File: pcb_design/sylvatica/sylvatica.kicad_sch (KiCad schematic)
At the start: 120 parts, among them J1 USB_C_Receptacle, J2 USB_C_Receptacle, J3 USB_C_Receptacle, J4 USB_C_Receptacle, J5 Conn_02x13_Odd_Even, J6 Conn_01x04_Female, J7 Conn_01x06_Female, J9 Conn_01x06_Female, Q1 Q_NMOS_GSD, Q2 Q_NMOS_GSD, SW1 SW_Push, U1 PGA113, U10 dsPIC33EP512MC806, U11 SiP32431, U12 LP2985-5.0, U13 REF2033, U14 OPA320, U15 SiP32431, U16 SiP32431, U17 SiP32431, U18 SiP32431, U19 ADM7170, U2 PGA113, U20 MCP2542FD, U21 TPS737, U22 SiP32431, U3 PGA113, U4 PGA113, U5 PGA113, U6 PGA113, U7 PGA113, U8 PGA113, U9 ADS8332, Y1 Crystal_GND24

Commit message: Update.
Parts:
- added J8: Conn_01x04_Female, Connector_PinSocket_2.54mm:PinSocket_1x04_P2.54mm_Vertical, symbol Connector:Conn_01x04_Female
- C20: symbol Device:CP -> Device:C
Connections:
- net BLINK: now also U10.63 (AN27PWM2H/PMD3/RPI83/RE3); no longer U10.64 (AN28/PWM3L/PMD4/RP84/RE4)
- net EV1: now also J1.A7 (D-), J1.B7 (D-); no longer J1.A10 (RX2-), J1.B10 (RX1-)
- net EV2: now also J2.A7 (D-), J2.B7 (D-); no longer J2.A10 (RX2-), J2.B10 (RX1-)
- net EV3: now also J3.A7 (D-), J3.B7 (D-); no longer J3.A10 (RX2-), J3.B10 (RX1-)
- net EV4: now also J4.A7 (D-), J4.B7 (D-); no longer J4.A10 (RX2-), J4.B10 (RX1-)
- net OW1: now also J1.A6 (D+), J1.B6 (D+), U10.22 (AN9/PMA7/RPI41/RB9); no longer J1.A3 (TX1-), J1.B3 (TX2-)
- net OW2: now also J2.A6 (D+), J2.B6 (D+), U10.21 (AN8/PMA6/RPI40/RB8); no longer J2.A3 (TX1-), J2.B3 (TX2-)
- net OW3: now also J3.A6 (D+), J3.B6 (D+), U10.11 (AN5/C1IN1+/RPI37/RB5); no longer J3.A3 (TX1-), J3.B3 (TX2-)
- net OW4: now also J4.A6 (D+), J4.B6 (D+), U10.64 (AN28/PWM3L/PMD4/RP84/RE4); no longer J4.A3 (TX1-), J4.B3 (TX2-)
- net REF_C2: now also U10.27 (TCK/AN12/PMA11/RPI44/RB12); no longer U10.29 (AN14/PMA1/RPI46/RB14)
- net SCL1: now also J1.A10 (RX2-), J1.B10 (RX1-), J2.A10 (RX2-), J2.B10 (RX1-), J3.A10 (RX2-), J3.B10 (RX1-), J4.A10 (RX2-), J4.B10 (RX1-); no longer J1.A7 (D-), J1.B7 (D-), J2.A7 (D-), J2.B7 (D-), J3.A7 (D-), J3.B7 (D-), J4.A7 (D-), J4.B7 (D-)
- net SDA1: now also J1.A3 (TX1-), J1.B3 (TX2-), J2.A3 (TX1-), J2.B3 (TX2-), J3.A3 (TX1-), J3.B3 (TX2-), J4.A3 (TX1-), J4.B3 (TX2-); no longer J1.A6 (D+), J1.B6 (D+), J2.A6 (D+), J2.B6 (D+), J3.A6 (D+), J3.B6 (D+), J4.A6 (D+), J4.B6 (D+)
- net S_PS_SW2: now also U10.15 (PGEC3/AN1/VREF-/RPI33/RB1); no longer U10.12 (AN4/C1IN2-/RPI36/RB4)
- net ~{INT2}: now also U10.16 (PGED3/AN0/VREF+/RPI32/RB0); no longer U10.13 (AN3/C2IN1+/VPIO/RPI35/RB3)
- net OW5: now reaches U10.23 (TMS/AN10/PMA13/RPI42/RB10)
- net OW5: now also J8.1 (Pin_1)
- net OW6: now reaches U10.28 (TDI/AN13/PMA10/RPI45/RB13)
- net OW6: now also J8.2 (Pin_2)
- net +3V3 renamed +3.3V
- net AS_PS renamed S_PS
- net AS_PS2 renamed S_PS2
- net CAN_C1: no longer names the net of J5.23 (Pin_23)
- net PGM: no longer names the net of J9.6 (Pin_6)
- new net OW7: J8.3 (Pin_3), U10.12 (AN4/C1IN2-/RPI36/RB4)
- new net OW8: J8.4 (Pin_4), U10.13 (AN3/C2IN1+/VPIO/RPI35/RB3)
- no-connect marks 4 -> 39
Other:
- moved on the sheet: C45

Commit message: New and updated board designs.
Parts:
- removed J5: Conn_02x13_Odd_Even, Connector_PinHeader_2.54mm:PinHeader_2x13_P2.54mm_Vertical, symbol Connector_Generic:Conn_02x13_Odd_Even
- removed J6, J8: Conn_01x04_Female, Connector_PinSocket_2.54mm:PinSocket_1x04_P2.54mm_Vertical, symbol Connector:Conn_01x04_Female
- removed J7: Conn_01x06_Female, Connector_PinSocket_2.54mm:PinSocket_1x06_P2.54mm_Vertical, symbol Connector:Conn_01x06_Female
- removed R16: 10k, Resistor_SMD:R_0603_1608Metric, symbol Device:R
- added C63: 4.7nF, Capacitor_SMD:C_0603_1608Metric, symbol Device:C
- added J5, J6: Conn_02x07_Odd_Even, samtec:SAMTEC_TMMH-107-01-T-DV, symbol Connector_Generic:Conn_02x07_Odd_Even
- added R11: 60R, Resistor_SMD:R_0603_1608Metric, symbol Device:R
- added R8: 1k, Resistor_SMD:R_0603_1608Metric, symbol Device:R
- N1: footprint board:Enclosure-Gloxinia2 -> board:Enclosure-Gloxinia4
- Q2: Mouser 512-BSS138 -> 771-PMV20XNER; Price 0.16 -> (none)
- R15: value 10k -> 60R; Mouser 284-APC0603B10K0N -> 594-5063JD120R0F; Price 0.068 -> 0.099
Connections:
- net +3.3V: now also J5.10 (Pin_10); no longer Q2.1 (G), R15.1
- net +4V: now also U13.3 (EN)
- net AS_PS_SW2: now also U10.16 (PGED3/AN0/VREF+/RPI32/RB0); no longer U10.14 (AN2/C2IN2-/VMIO/RPI34/RB2)
- net CAN_H: now also Q2.3 (D), J5.3 (Pin_3)
- net CAN_L: now also R15.1, J5.5 (Pin_5)
- net CTS: now also J5.4 (Pin_4)
- net EV5: now also J6.8 (Pin_8)
- net EV6: now also J6.10 (Pin_10)
- net EV7: now also J6.12 (Pin_12)
- net EV8: now also J6.14 (Pin_14)
- net GND: now also C63.2, J5.11 (Pin_11), J5.12 (Pin_12), J5.13 (Pin_13), J5.14 (Pin_14), J6.2 (Pin_2), J6.4 (Pin_4)
- net OW5: now also U10.29 (AN14/PMA1/RPI46/RB14), J6.7 (Pin_7); no longer U10.23 (TMS/AN10/PMA13/RPI42/RB10)
- net OW6: now also J6.9 (Pin_9)
- net OW7: now also J6.11 (Pin_11)
- net OW8: now also J6.13 (Pin_13)
- net RTS: now also J5.2 (Pin_2)
- net RXD: now also J5.8 (Pin_8)
- net SCL2: now also J6.3 (Pin_3)
- net SDA2: now also J6.5 (Pin_5)
- net S_PS2: now also J6.1 (Pin_1)
- net TXD: now also J5.6 (Pin_6)
- net VBUS: now also J5.1 (Pin_1)
- net ~{INT2}: now also U10.23 (TMS/AN10/PMA13/RPI42/RB10), J6.6 (Pin_6); no longer U10.16 (PGED3/AN0/VREF+/RPI32/RB0)
- net CAN_C1: now reaches U10.8 (C2IN1-/PMA2/RPI121/RG9)
- net CAN_C1: now also J5.7 (Pin_7)
- removed net EN_REF: Q2.2 (S), R15.2, U10.24 (TDO/AN11/PMA12/RPI43/RB11)
- removed net EN_REF3.3: Q2.3 (D), U13.3 (EN)
- new net: Q2.1 (G), R8.1
- new net: Q2.2 (S), R11.2
- new net: C63.1, R11.1, R15.2
- new net CAN_C2: J5.9 (Pin_9), U10.14 (AN2/C2IN2-/VMIO/RPI34/RB2)
- new net TERM: R8.2, U10.24 (TDO/AN11/PMA12/RPI43/RB11)
- no-connect marks 39 -> 26

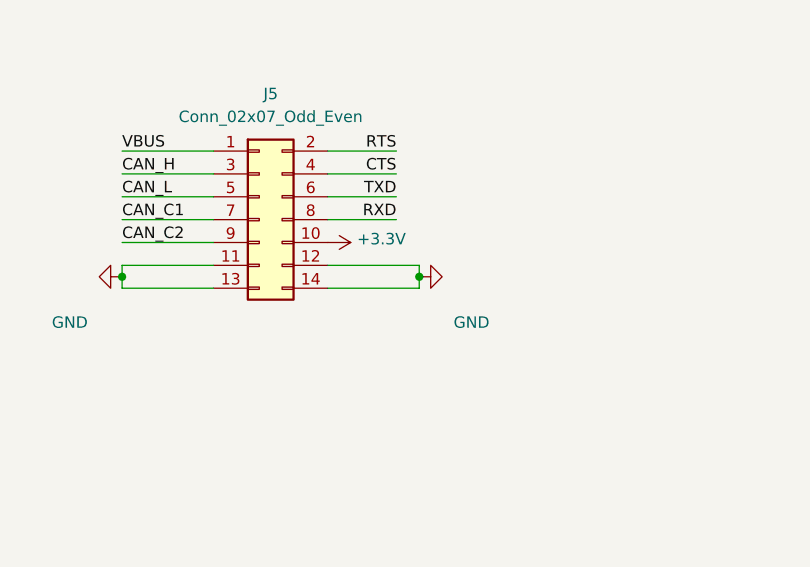
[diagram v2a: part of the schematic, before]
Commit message: Expose RTCC pin for synchronisation
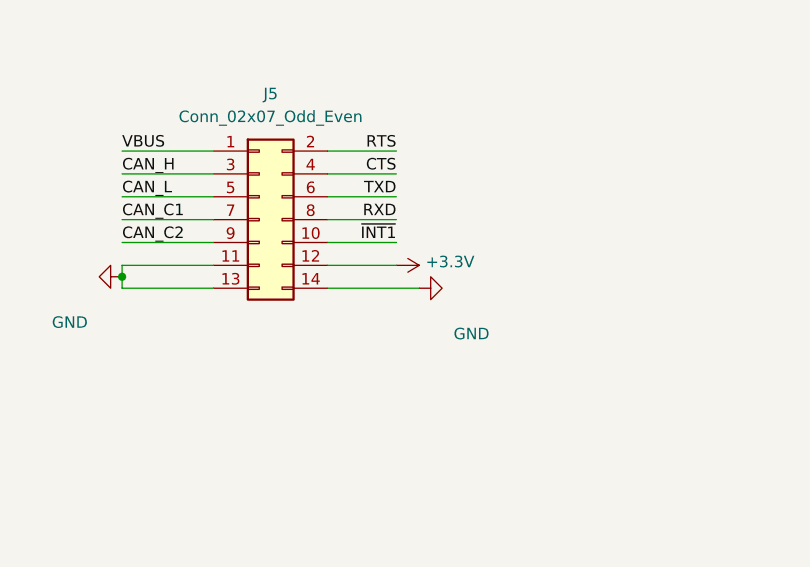
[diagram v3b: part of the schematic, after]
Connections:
- net +3.3V: now also J5.12 (Pin_12); no longer J5.10 (Pin_10)
- net GND: no longer J5.12 (Pin_12)
- net ~{INT1}: now also J5.10 (Pin_10)
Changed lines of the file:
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@@
   (junction (at 306.07 35.56) (diameter 0) (color 0 0 0 0)
   )
-  (junction (at 323.85 326.39) (diameter 0) (color 0 0 0 0)
-  )
   (junction (at 252.73 19.05) (diameter 0) (color 0 0 0 0)
   )
@@
     (stroke (width 0) (type default) (color 0 0 0 0))
   )
+  (wire (pts (xy 313.69 325.12) (xy 321.31 325.12))
+    (stroke (width 0) (type default) (color 0 0 0 0))
+  )
   (wire (pts (xy 317.5 130.81) (xy 317.5 132.08))
     (stroke (width 0) (type default) (color 0 0 0 0))
@@
     (stroke (width 0) (type default) (color 0 0 0 0))
   )
-  (wire (pts (xy 323.85 326.39) (xy 323.85 327.66))
-    (stroke (width 0) (type default) (color 0 0 0 0))
-  )
   (wire (pts (xy 303.53 123.19) (xy 323.85 123.19))
     (stroke (width 0) (type default) (color 0 0 0 0))
@@
     (stroke (width 0) (type default) (color 0 0 0 0))
   )
-  (wire (pts (xy 323.85 325.12) (xy 313.69 325.12))
-    (stroke (width 0) (type default) (color 0 0 0 0))
-  )
   (wire (pts (xy 173.99 120.65) (xy 171.45 120.65))
     (stroke (width 0) (type default) (color 0 0 0 0))
@@
     (stroke (width 0) (type default) (color 0 0 0 0))
   )
+  (wire (pts (xy 313.69 322.58) (xy 321.31 322.58))
+    (stroke (width 0) (type default) (color 0 0 0 0))
+  )
   (wire (pts (xy 156.21 184.15) (xy 153.67 184.15))
     (stroke (width 0) (type default) (color 0 0 0 0))
@@
     (stroke (width 0) (type default) (color 0 0 0 0))
   )
-  (wire (pts (xy 323.85 325.12) (xy 323.85 326.39))
-    (stroke (width 0) (type default) (color 0 0 0 0))
-  )
   (wire (pts (xy 226.06 19.05) (xy 234.95 19.05))
     (stroke (width 0) (type default) (color 0 0 0 0))
@@
     (effects (font (size 1.27 1.27)) (justify right bottom))
   )
+  (label "~{INT1}" (at 321.31 322.58 180)
+    (effects (font (size 1.27 1.27)) (justify right bottom))
+  )
   (label "S_PS" (at 436.88 281.94 180)
     (effects (font (size 1.27 1.27)) (justify right bottom))
@@
     (pin "1")
   )
-  (symbol (lib_id "power:+3.3V") (at 313.69 322.58 270) (mirror x) (unit 1)
+  (symbol (lib_id "power:+3.3V") (at 321.31 325.12 270) (mirror x) (unit 1)
     (in_bom yes) (on_board yes)
-    (property "Reference" "#PWR026" (id 0) (at 309.88 322.58 0)
+    (property "Reference" "#PWR026" (id 0) (at 317.5 325.12 0)
       (effects (font (size 1.27 1.27)) hide)
     )
-    (property "Value" "+3.3V" (id 1) (at 316.9412 322.199 90)
+    (property "Value" "+3.3V" (id 1) (at 324.5612 324.739 90)
       (effects (font (size 1.27 1.27)) (justify left))
     )
-    (property "Footprint" "" (id 2) (at 313.69 322.58 0)
+    (property "Footprint" "" (id 2) (at 321.31 325.12 0)
       (effects (font (size 1.27 1.27)) hide)
     )
-    (property "Datasheet" "" (id 3) (at 313.69 322.58 0)
+    (property "Datasheet" "" (id 3) (at 321.31 325.12 0)
       (effects (font (size 1.27 1.27)) hide)
     )
@@
     (pin "1")
   )
-  (symbol (lib_id "power:GND") (at 323.85 326.39 90) (mirror x) (unit 1)
+  (symbol (lib_id "power:GND") (at 323.85 327.66 90) (mirror x) (unit 1)
     (in_bom yes) (on_board yes)
-    (property "Reference" "#PWR027" (id 0) (at 330.2 326.39 0)
+    (property "Reference" "#PWR027" (id 0) (at 330.2 327.66 0)
       (effects (font (size 1.27 1.27)) hide)
     )
-    (property "Value" "GND" (id 1) (at 327.66 331.4699 90)
+    (property "Value" "GND" (id 1) (at 327.66 332.7399 90)
       (effects (font (size 1.27 1.27)) (justify right))
     )
-    (property "Footprint" "" (id 2) (at 323.85 326.39 0)
+    (property "Footprint" "" (id 2) (at 323.85 327.66 0)
       (effects (font (size 1.27 1.27)) hide)
     )
-    (property "Datasheet" "" (id 3) (at 323.85 326.39 0)
+    (property "Datasheet" "" (id 3) (at 323.85 327.66 0)
       (effects (font (size 1.27 1.27)) hide)
     )
